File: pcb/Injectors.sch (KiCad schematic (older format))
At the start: 48 parts, among them Q1 VND14NV04, Q2 VND14NV04, Q3 VND14NV04, Q4 VND14NV04, Q5 VND14NV04, Q6 VND14NV04, Q7 VND14NV04, Q8 VND14NV04

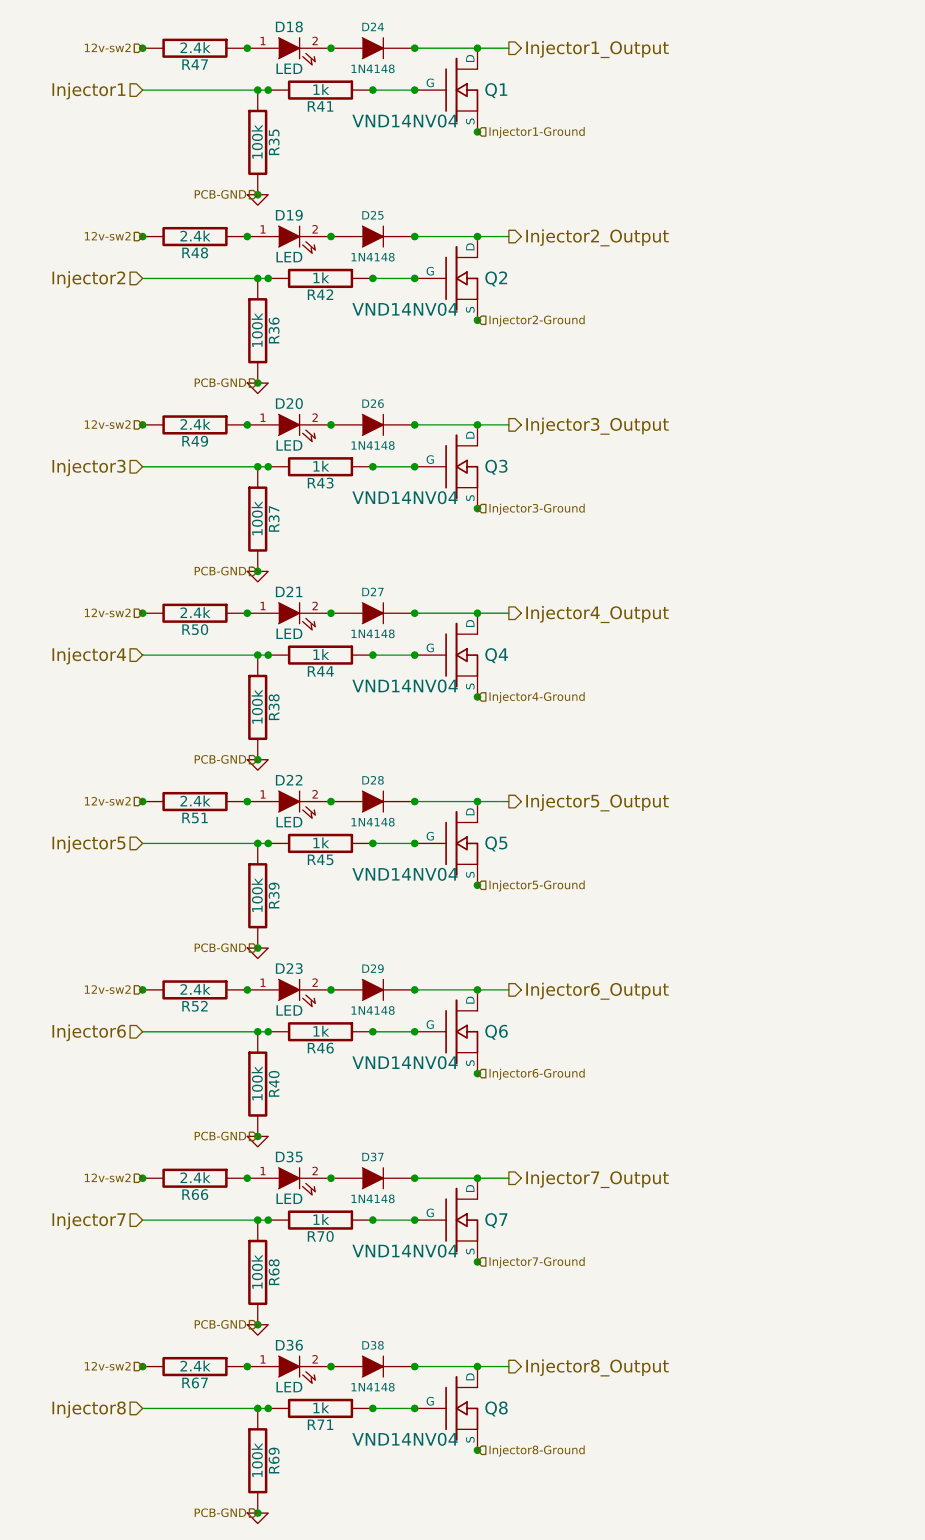
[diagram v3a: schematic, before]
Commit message: Connected all Injector MOSFET ground connection points together, added PNP transistor, removed HCPL optocoupler ICs
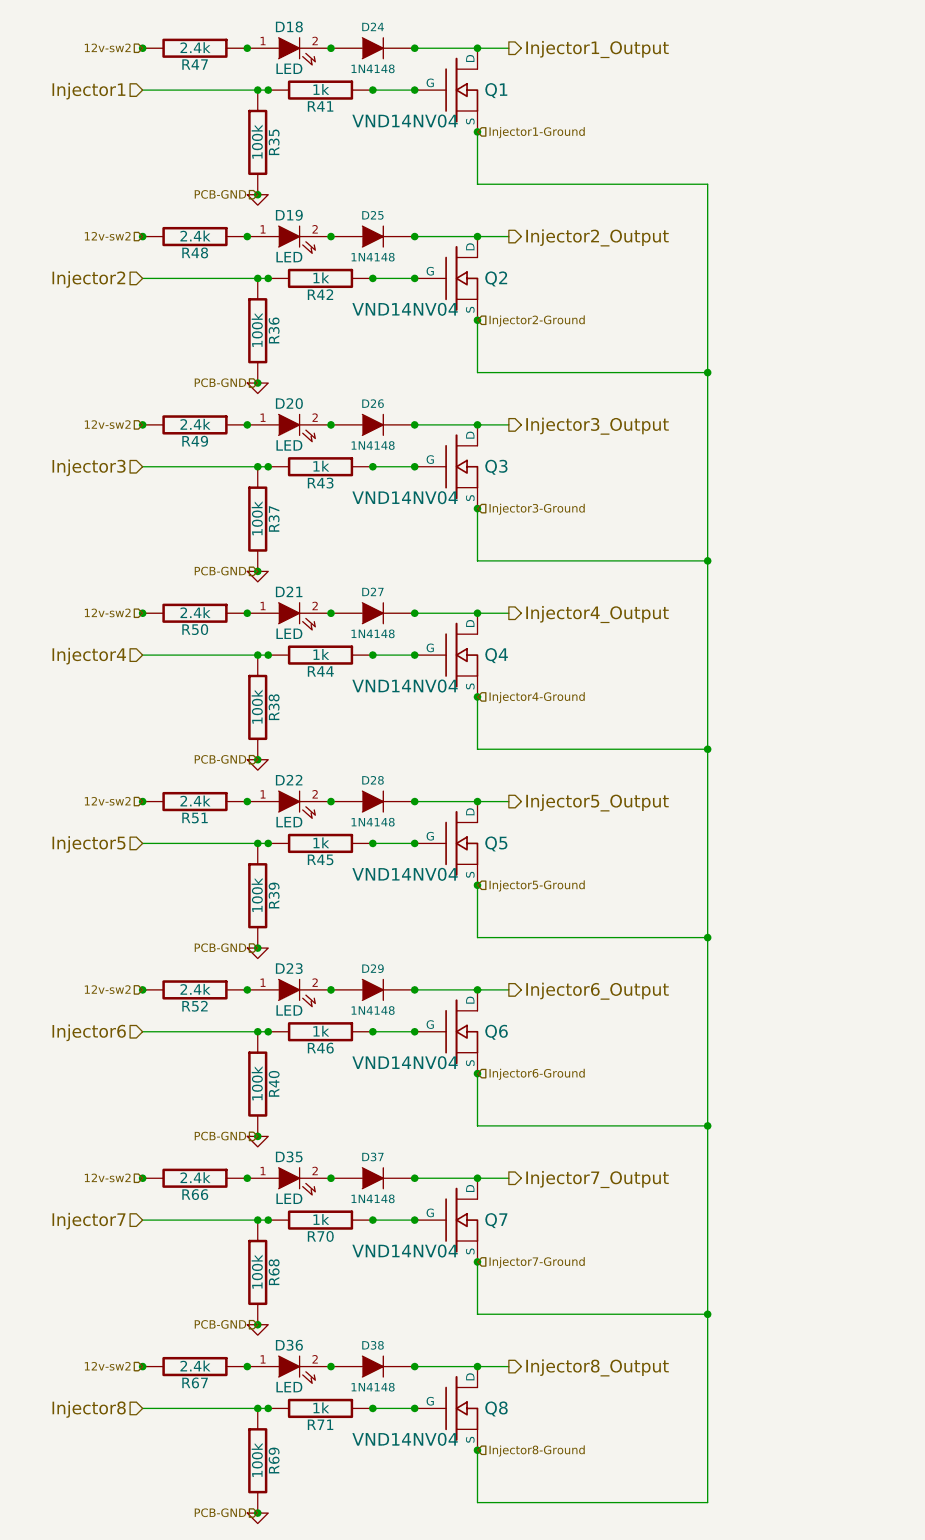
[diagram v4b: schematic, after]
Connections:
- net Injector2-Ground is gone; now on net Injector1-Ground: Q2.S
- net Injector3-Ground is gone; now on net Injector1-Ground: Q3.S
- net Injector4-Ground is gone; now on net Injector1-Ground: Q4.S
- net Injector5-Ground is gone; now on net Injector1-Ground: Q5.S
- net Injector6-Ground is gone; now on net Injector1-Ground: Q6.S
- net Injector7-Ground is gone; now on net Injector1-Ground: Q7.S
- net Injector8-Ground is gone; now on net Injector1-Ground: Q8.S
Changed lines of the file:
@@
-EESchema Schematic File Version 2  date Fri 06 Jul 2012 11:19:11 PM EDT
+EESchema Schematic File Version 2  date Sun 08 Jul 2012 04:36:18 PM EDT
 LIBS:opto
 LIBS:Jaguar
 LIBS:power
 LIBS:conn
+LIBS:transistors
 LIBS:Jaguar-cache
 EELAYER 24  0
@@
 Sheet 6 7
 Title "Jaguar PCB for FreeEMS"
-Date "6 jul 2012"
+Date "8 jul 2012"
 Rev "A4"
 Comp "diyefi.org"
@@
 Comment4 ""
 $EndDescr
+Connection ~ 5100 6750
+Wire Wire Line
+	5100 7650 5100 1350
+Wire Wire Line
+	5100 7650 4000 7650
+Wire Wire Line
+	4000 7650 4000 7400
+Connection ~ 5100 4950
+Wire Wire Line
+	5100 5850 4000 5850
+Wire Wire Line
+	4000 5850 4000 5600
+Connection ~ 5100 3150
+Wire Wire Line
+	5100 4050 4000 4050
+Wire Wire Line
+	4000 4050 4000 3800
+Wire Wire Line
+	4000 1100 4000 1350
+Wire Wire Line
+	4000 2000 4000 2250
+Wire Wire Line
+	4000 2250 5100 2250
+Connection ~ 3700 7000
+Connection ~ 2950 7700
+Wire Wire Line
+	3700 7200 3500 7200
+Connection ~ 4000 7000
+Connection ~ 4000 7400
+Connection ~ 3700 7200
+Connection ~ 3500 7200
+Connection ~ 3000 7200
+Connection ~ 2950 7200
+Connection ~ 2900 7000
+Connection ~ 3300 7000
+Connection ~ 2400 7000
+Wire Wire Line
+	2400 7200 3000 7200
+Wire Wire Line
+	3700 7000 4150 7000
+Wire Wire Line
+	3700 6100 4150 6100
+Wire Wire Line
+	2400 6300 3000 6300
+Connection ~ 2400 6100
+Connection ~ 3300 6100
+Connection ~ 2900 6100
+Connection ~ 2950 6300
+Connection ~ 3000 6300
+Connection ~ 3500 6300
+Connection ~ 3700 6300
+Connection ~ 4000 6500
+Connection ~ 4000 6100
+Wire Wire Line
+	3700 6300 3500 6300
+Connection ~ 2950 6800
+Connection ~ 3700 6100
+Wire Wire Line
+	3000 1800 2400 1800
+Wire Wire Line
+	2400 900  3000 900
+Connection ~ 3700 5200
+Connection ~ 3700 4300
+Wire Wire Line
+	3700 4300 4150 4300
+Wire Wire Line
+	3700 2500 4150 2500
+Wire Wire Line
+	3000 2700 2400 2700
+Wire Wire Line
+	2400 3600 3000 3600
+Wire Wire Line
+	3000 4500 2400 4500
+Connection ~ 4000 700
+Connection ~ 2950 5900
+Wire Wire Line
+	3700 5400 3500 5400
+Connection ~ 4000 5200
+Connection ~ 4000 5600
+Connection ~ 3700 5400
+Connection ~ 3500 5400
+Connection ~ 3000 5400
+Connection ~ 2950 5400
+Connection ~ 2950 4500
+Connection ~ 3000 4500
+Connection ~ 3500 4500
+Connection ~ 3700 4500
+Connection ~ 4000 4700
+Connection ~ 4000 4300
+Wire Wire Line
+	3700 4500 3500 4500
+Connection ~ 2950 5000
+Connection ~ 2950 4100
+Wire Wire Line
+	3700 3600 3500 3600
+Connection ~ 4000 3400
+Connection ~ 4000 3800
+Connection ~ 3700 3600
+Connection ~ 3500 3600
+Connection ~ 3000 3600
+Connection ~ 2950 3600
+Connection ~ 2950 3200
+Wire Wire Line
+	3700 2700 3500 2700
+Connection ~ 4000 2500
+Connection ~ 4000 2900
+Connection ~ 3700 2700
+Connection ~ 3500 2700
+Connection ~ 3000 2700
+Connection ~ 2950 2700
+Connection ~ 2950 2300
+Wire Wire Line
+	3700 1800 3500 1800
+Connection ~ 4000 1600
+Connection ~ 4000 2000
+Connection ~ 3700 1800
+Connection ~ 3500 1800
+Connection ~ 3000 1800
+Connection ~ 2950 1800
+Connection ~ 2950 900
+Connection ~ 3000 900
+Connection ~ 3500 900
+Connection ~ 3700 900
+Connection ~ 4000 1100
+Wire Wire Line
+	3700 900  3500 900
+Connection ~ 2950 1400
+Connection ~ 3300 700
+Connection ~ 2900 700
+Connection ~ 2900 1600
+Connection ~ 3300 1600
+Connection ~ 3300 2500
+Connection ~ 2900 2500
+Connection ~ 2900 3400
+Connection ~ 3300 3400
+Connection ~ 3300 4300
+Connection ~ 2900 4300
+Connection ~ 2900 5200
+Connection ~ 3300 5200
+Connection ~ 3700 700
+Connection ~ 3700 1600
+Connection ~ 2400 5200
+Wire Wire Line
+	2400 5400 3000 5400
+Connection ~ 2400 4300
+Connection ~ 2400 3400
+Wire Wire Line
+	3700 3400 4150 3400
+Connection ~ 3700 3400
+Connection ~ 3700 2500
+Wire Wire Line
+	3700 700  4150 700
+Connection ~ 2400 700
+Connection ~ 2400 1600
+Connection ~ 2400 2500
+Wire Wire Line
+	3700 5200 4150 5200
+Wire Wire Line
+	3700 1600 4150 1600
+Wire Wire Line
+	4000 1350 5100 1350
+Wire Wire Line
+	4000 2900 4000 3150
+Wire Wire Line
+	4000 3150 5100 3150
+Connection ~ 5100 2250
+Wire Wire Line
+	4000 4700 4000 4950
+Wire Wire Line
+	4000 4950 5100 4950
+Connection ~ 5100 4050
+Wire Wire Line
+	4000 6500 4000 6750
+Wire Wire Line
+	4000 6750 5100 6750
+Connection ~ 5100 5850
 Text HLabel 4000 7400 2    40   Input ~ 0
 Injector8-Ground
@@
 	1    0    0    -1
 $EndComp
-Wire Wire Line
-	3700 1600 4150 1600
-Wire Wire Line
-	3700 5200 4150 5200
-Connection ~ 2400 2500
-Connection ~ 2400 1600
-Connection ~ 2400 700
-Wire Wire Line
-	3700 700  4150 700
-Connection ~ 3700 2500
-Connection ~ 3700 3400
-Wire Wire Line
-	3700 3400 4150 3400
-Connection ~ 2400 3400
-Connection ~ 2400 4300
-Wire Wire Line
-	2400 5400 3000 5400
-Connection ~ 2400 5200
-Connection ~ 3700 1600
-Connection ~ 3700 700
-Connection ~ 3300 5200
-Connection ~ 2900 5200
-Connection ~ 2900 4300
-Connection ~ 3300 4300
-Connection ~ 3300 3400
-Connection ~ 2900 3400
-Connection ~ 2900 2500
-Connection ~ 3300 2500
-Connection ~ 3300 1600
-Connection ~ 2900 1600
-Connection ~ 2900 700
-Connection ~ 3300 700
-Connection ~ 2950 1400
-Wire Wire Line
-	3700 900  3500 900
-Connection ~ 4000 1100
-Connection ~ 3700 900
-Connection ~ 3500 900
-Connection ~ 3000 900
-Connection ~ 2950 900
-Connection ~ 2950 1800
-Connection ~ 3000 1800
-Connection ~ 3500 1800
-Connection ~ 3700 1800
-Connection ~ 4000 2000
-Connection ~ 4000 1600
-Wire Wire Line
-	3700 1800 3500 1800
-Connection ~ 2950 2300
-Connection ~ 2950 2700
-Connection ~ 3000 2700
-Connection ~ 3500 2700
-Connection ~ 3700 2700
-Connection ~ 4000 2900
-Connection ~ 4000 2500
-Wire Wire Line
-	3700 2700 3500 2700
-Connection ~ 2950 3200
-Connection ~ 2950 3600
-Connection ~ 3000 3600
-Connection ~ 3500 3600
-Connection ~ 3700 3600
-Connection ~ 4000 3800
-Connection ~ 4000 3400
-Wire Wire Line
-	3700 3600 3500 3600
-Connection ~ 2950 4100
-Connection ~ 2950 5000
-Wire Wire Line
-	3700 4500 3500 4500
-Connection ~ 4000 4300
-Connection ~ 4000 4700
-Connection ~ 3700 4500
-Connection ~ 3500 4500
-Connection ~ 3000 4500
-Connection ~ 2950 4500
-Connection ~ 2950 5400
-Connection ~ 3000 5400
-Connection ~ 3500 5400
-Connection ~ 3700 5400
-Connection ~ 4000 5600
-Connection ~ 4000 5200
-Wire Wire Line
-	3700 5400 3500 5400
-Connection ~ 2950 5900
-Connection ~ 4000 700
-Wire Wire Line
-	3000 4500 2400 4500
-Wire Wire Line
-	2400 3600 3000 3600
-Wire Wire Line
-	3000 2700 2400 2700
-Wire Wire Line
-	3700 2500 4150 2500
-Wire Wire Line
-	3700 4300 4150 4300
-Connection ~ 3700 4300
-Connection ~ 3700 5200
-Wire Wire Line
-	2400 900  3000 900
-Wire Wire Line
-	3000 1800 2400 1800
-Connection ~ 3700 6100
-Connection ~ 2950 6800
-Wire Wire Line
-	3700 6300 3500 6300
-Connection ~ 4000 6100
-Connection ~ 4000 6500
-Connection ~ 3700 6300
-Connection ~ 3500 6300
-Connection ~ 3000 6300
-Connection ~ 2950 6300
-Connection ~ 2900 6100
-Connection ~ 3300 6100
-Connection ~ 2400 6100
-Wire Wire Line
-	2400 6300 3000 6300
-Wire Wire Line
-	3700 6100 4150 6100
-Wire Wire Line
-	3700 7000 4150 7000
-Wire Wire Line
-	2400 7200 3000 7200
-Connection ~ 2400 7000
-Connection ~ 3300 7000
-Connection ~ 2900 7000
-Connection ~ 2950 7200
-Connection ~ 3000 7200
-Connection ~ 3500 7200
-Connection ~ 3700 7200
-Connection ~ 4000 7400
-Connection ~ 4000 7000
-Wire Wire Line
-	3700 7200 3500 7200
-Connection ~ 2950 7700
-Connection ~ 3700 7000
 $Comp
 L GND #PWR039

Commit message: Changed Injector MOSFET grounds to be in pairs with a 0.0700" trace between them instead of a 0.0350" trace like the Injector outputs have
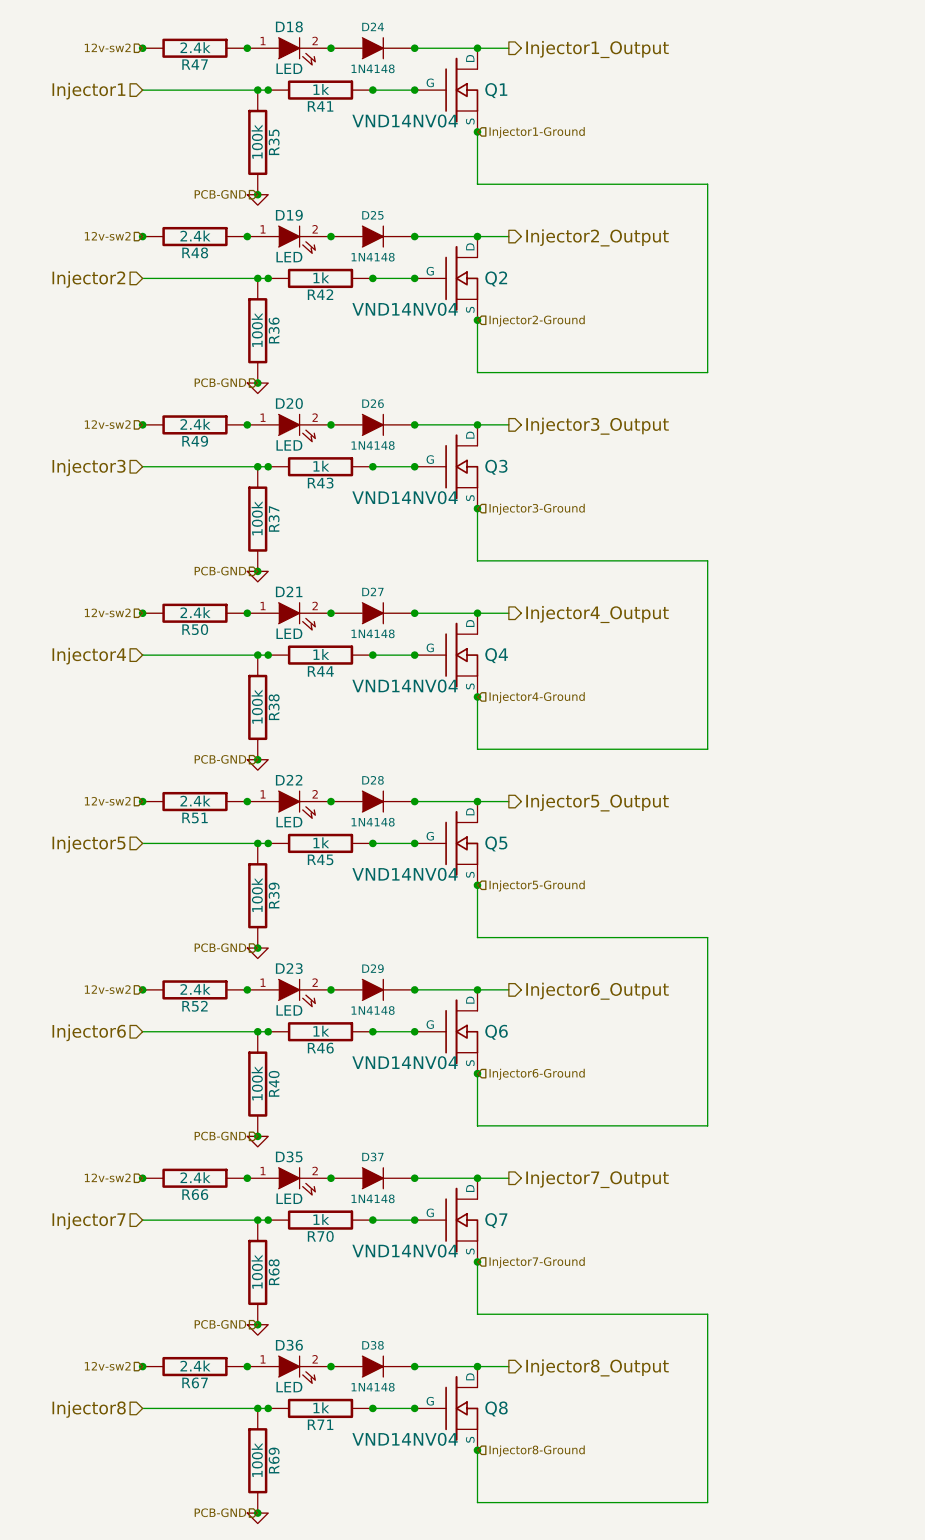
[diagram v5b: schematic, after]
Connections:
- net Injector1-Ground: no longer Q3.S, Q4.S, Q5.S, Q6.S, Q7.S, Q8.S
- new net Injector3-Ground: Q3.S, Q4.S
- new net Injector5-Ground: Q5.S, Q6.S
- new net Injector7-Ground: Q7.S, Q8.S
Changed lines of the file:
@@
-EESchema Schematic File Version 2  date Sun 08 Jul 2012 04:36:18 PM EDT
+EESchema Schematic File Version 2  date Sun 08 Jul 2012 05:17:31 PM EDT
 LIBS:opto
 LIBS:Jaguar
@@
 Comment4 ""
 $EndDescr
-Connection ~ 5100 6750
 Wire Wire Line
-	5100 7650 5100 1350
+	5100 7650 5100 6750
+Wire Wire Line
+	5100 4050 5100 3150
 Wire Wire Line
 	5100 7650 4000 7650
 Wire Wire Line
 	4000 7650 4000 7400
-Connection ~ 5100 4950
 Wire Wire Line
-	5100 5850 4000 5850
+	4000 5850 5100 5850
 Wire Wire Line
 	4000 5850 4000 5600
-Connection ~ 5100 3150
 Wire Wire Line
 	5100 4050 4000 4050
@@
 Wire Wire Line
 	4000 3150 5100 3150
-Connection ~ 5100 2250
 Wire Wire Line
 	4000 4700 4000 4950
 Wire Wire Line
 	4000 4950 5100 4950
-Connection ~ 5100 4050
 Wire Wire Line
 	4000 6500 4000 6750
 Wire Wire Line
 	4000 6750 5100 6750
-Connection ~ 5100 5850
+Wire Wire Line
+	5100 1350 5100 2250
+Wire Wire Line
+	5100 4950 5100 5850
 Text HLabel 4000 7400 2    40   Input ~ 0
 Injector8-Ground
